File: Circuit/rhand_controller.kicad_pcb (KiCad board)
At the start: 2 copper layers, 100 x 100 mm, 39 parts, among them P1 BLUETOOTH, P10 LV_ADC, P11 LW_ADC, P12 RU_ADC, P13 RV_ADC, P14 RW_ADC, P2 CONN_01X06, P3 Wall, P4 CW, P5 Enable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

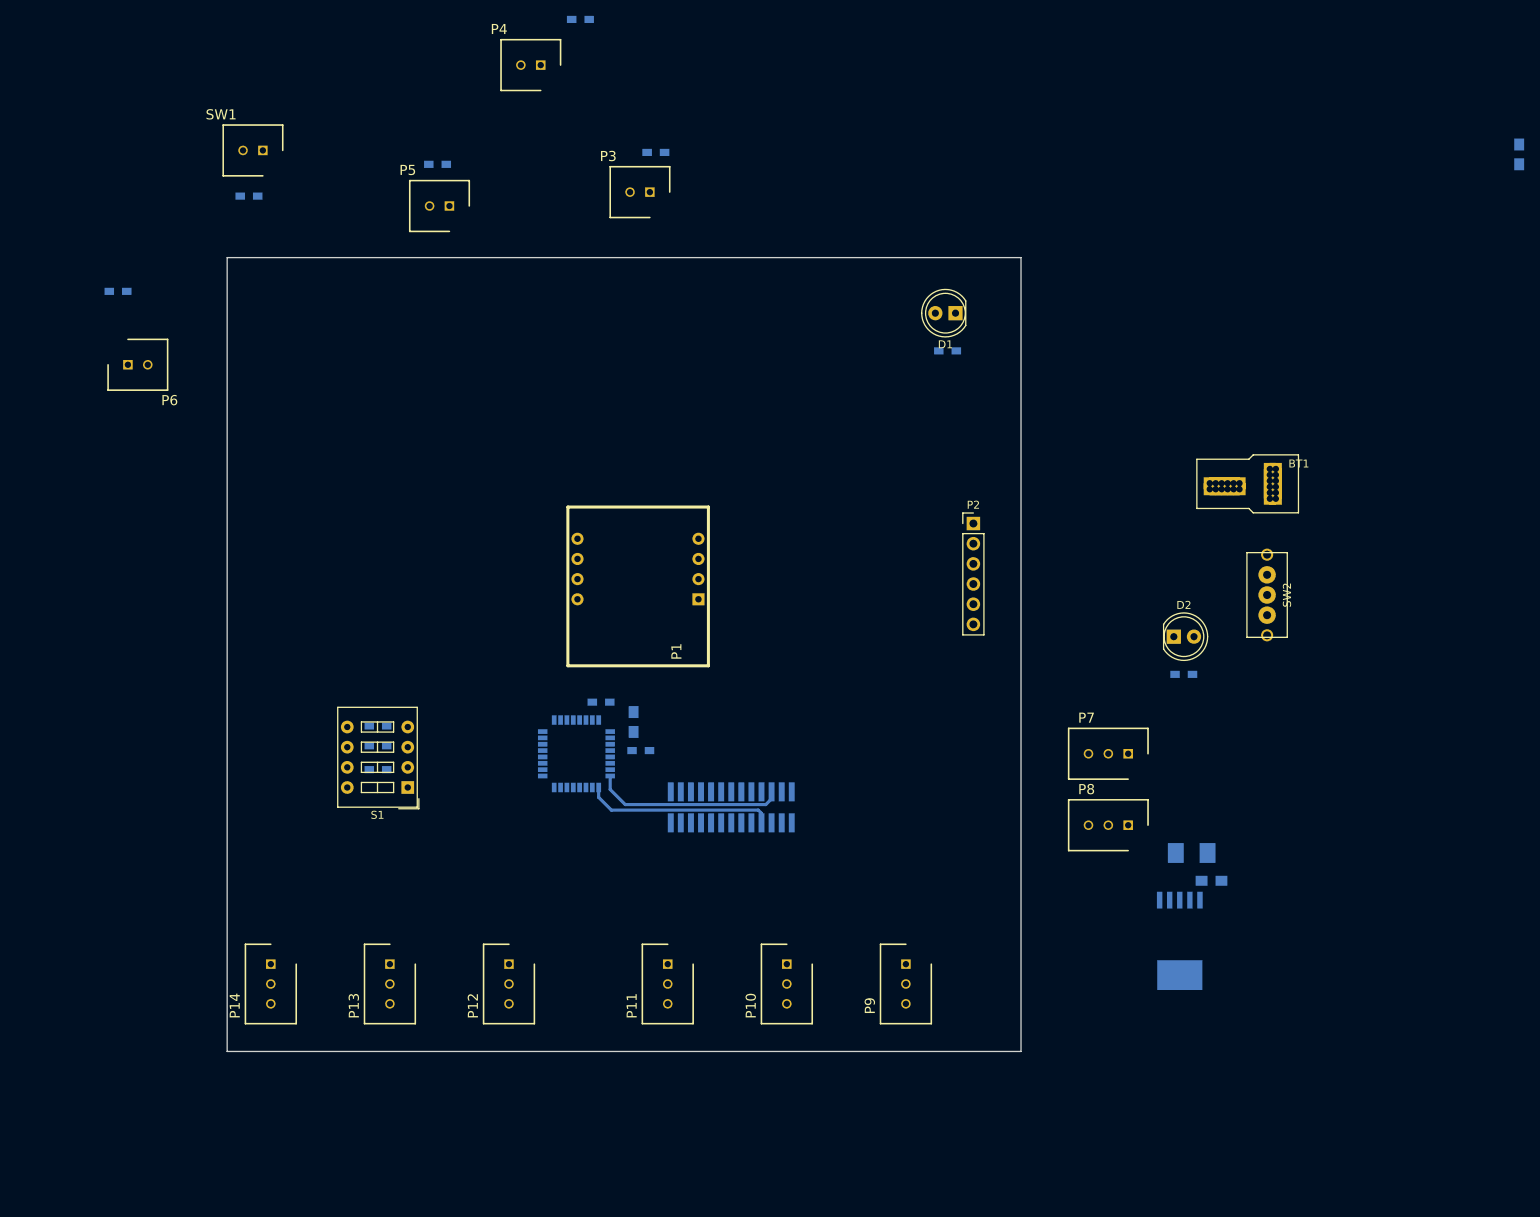
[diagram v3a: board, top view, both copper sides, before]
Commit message: ADCのピン配置修正と配線引きはじめ
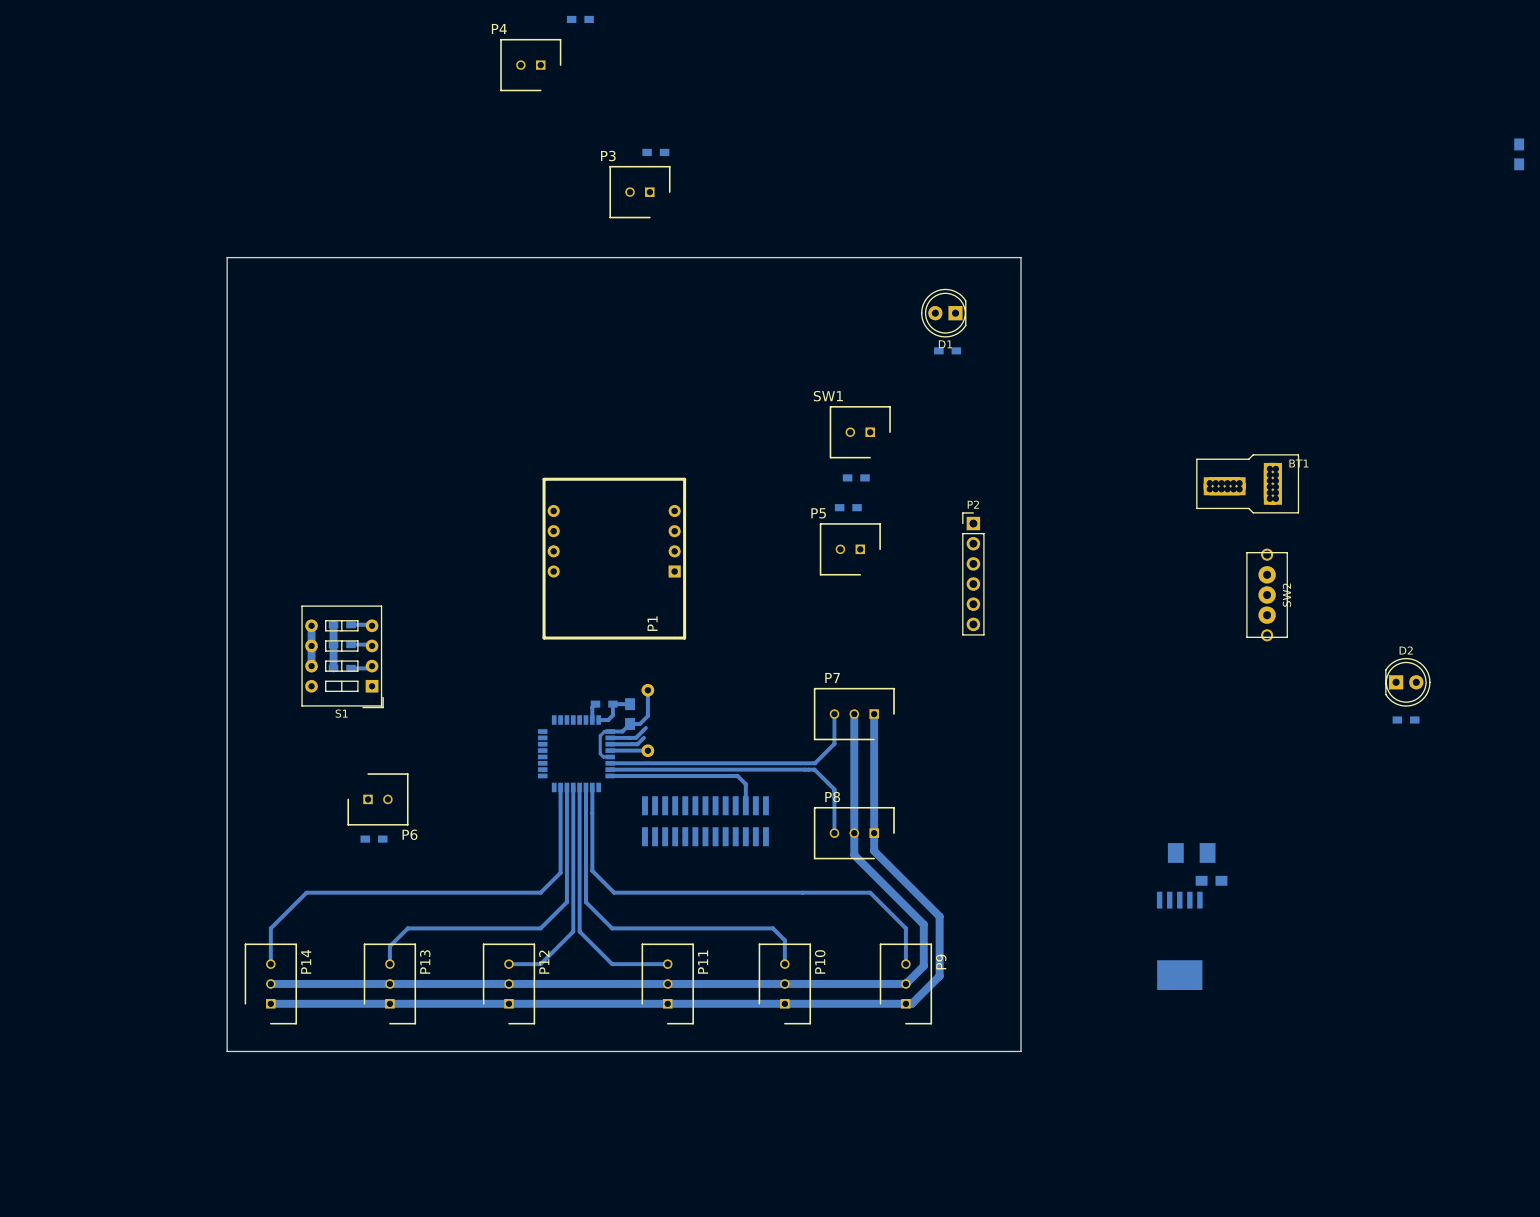
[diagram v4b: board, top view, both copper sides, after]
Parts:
- R7: footprint Resistors_SMD:R_0603_HandSoldering -> Resistors_ThroughHole:R_Axial_DIN0207_L6.3mm_D2.5mm_P7.62mm_Horizontal
- moved R4 84.3 mm to (129.2, 97.8)
- moved SW1 84.3 mm to (131.0, 92.0)
- moved R11 76.2 mm to (68.5, 143.2)
- moved P5 67.4 mm to (129.8, 106.8)
- moved R10 67.4 mm to (128.2, 101.5)
- moved P6 62.6 mm to (67.8, 138.2)
- moved P7 32.4 mm to (131.5, 127.5)
- moved P8 32.0 mm to (131.5, 142.5)
- moved D2 28.6 mm to (197.2, 123.5)
- moved R12 28.6 mm to (198.5, 128.2)
- moved R1 13.5 mm to (64.5, 116.2)
- moved R2 13.5 mm to (64.5, 118.8)
- moved R3 13.5 mm to (64.5, 121.8)
- moved S1 13.5 mm to (68.2, 124.0)
- moved R7 7.65 mm to (103.0, 124.5), turned to 270 degrees
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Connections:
- P10 pad 1: GND -> +3V3
- P10 pad 2: /LeftV -> GND
- P10 pad 3: +3V3 -> /LeftV
- P11 pad 1: GND -> +3V3
- P11 pad 2: /LeftW -> GND
- P11 pad 3: +3V3 -> /LeftW
- P12 pad 1: GND -> +3V3
- P12 pad 2: /RightU -> GND
- P12 pad 3: +3V3 -> /RightU
- P13 pad 1: GND -> +3V3
- P13 pad 2: /RightV -> GND
- P13 pad 3: +3V3 -> /RightV
- P14 pad 1: GND -> +3V3
- P14 pad 2: /RightW -> GND
- P14 pad 3: +3V3 -> /RightW
- P3 pad 1: GND -> /Wall
- P3 pad 2: /Wall -> GND
- P4 pad 1: GND -> /CW
- P4 pad 2: /CW -> GND
- P5 pad 1: GND -> /Enable
- P5 pad 2: /Enable -> GND
- P6 pad 1: GND -> /CCW
- P6 pad 2: /CCW -> GND
- P7 pad 1: GND -> +3V3
- P7 pad 2: /Joy_X -> GND
- P7 pad 3: +3V3 -> /Joy_X
- P8 pad 1: GND -> +3V3
- P8 pad 2: /Joy_Y -> GND
- P8 pad 3: +3V3 -> /Joy_Y
- P9 pad 1: GND -> +3V3
- P9 pad 2: /LeftU -> GND
- P9 pad 3: +3V3 -> /LeftU
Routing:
- net +3V3: track 0.00 -> 141.1 mm
- net GND: track 0.00 -> 129.7 mm
- net /LeftU: track 0.00 -> 57.5 mm
- net /RightW: track 0.00 -> 54.6 mm
- net /LeftV: track 0.00 -> 44.5 mm
- net /RightV: track 0.00 -> 41.3 mm
- net /Joy_Y: track 0.00 -> 34.8 mm
- net /Joy_X: track 0.00 -> 33.0 mm
- net /LeftW: track 0.00 -> 30.9 mm
- net /RightU: track 0.00 -> 27.9 mm
- net /315MHz_TXD: track 23.8 -> 0.00 mm
- net /Wall: track 0.00 -> 5.02 mm
- net /NRST: track 0.00 -> 4.76 mm
- net /Enable: track 0.00 -> 4.58 mm
- net /315MHz_RXD: track 24.0 -> 20.2 mm
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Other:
- net class Default: clearance 0.1 -> 0.15
- rule trace_clearance: 0.1 -> 0.15

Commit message: あらかた終わったぞ
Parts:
- R10, R11, R12, R4, R8, R9: footprint Resistors_SMD:R_0603_HandSoldering -> Resistors_ThroughHole:R_Axial_DIN0207_L6.3mm_D2.5mm_P7.62mm_Horizontal
- U1: moved to F.Cu
- moved P2 119.0 mm to (26.8, 123.5), turned to 90 degrees
- moved C1 114.9 mm to (118.2, 122.2), turned to 180 degrees
- moved R9 105.6 mm to (60.5, 140.0)
- moved P4 102.0 mm to (68.2, 145.5)
- moved U3 79.0 mm to (127.1, 85.1), turned to 270 degrees
- moved C3 77.7 mm to (131.0, 83.8), turned to 270 degrees
- moved BT1 72.4 mm to (113.4, 74.6)
- moved D2 71.3 mm to (139.0, 82.4), turned to 270 degrees
- moved C4 68.9 mm to (134.4, 87.0), turned to 90 degrees
- moved R4 68.5 mm to (60.8, 97.6), turned to 0 degrees
- moved SW1 65.3 mm to (65.8, 89.2), turned to 180 degrees
- moved SW2 64.9 mm to (127.7, 75.6), turned to 0 degrees
- moved R12 64.8 mm to (144.8, 92.0), turned to 180 degrees
- moved R8 61.5 mm to (142.2, 105.0)
- moved P3 47.6 mm to (134.7, 97.5), turned to 180 degrees
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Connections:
- U2 pad 29: /Blutooth_RXD -> /315MHz_RXD
- U2 pad 30: /Blutooth_TXD -> /315MHz_TXD
- U2 pad 8: /315MHz_RXD -> /Blutooth_RXD
- U2 pad 9: /315MHz_TXD -> /Blutooth_TXD
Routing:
- net GND: track 129.7 -> 349.0 mm
- net +3V3: track 141.1 -> 316.5 mm
- net /Wall: track 5.02 -> 61.2 mm
- net Net-(R4-Pad2): track 0.00 -> 48.5 mm
- net /Enable: track 4.58 -> 48.0 mm
- net /DSW_B2: track 2.70 -> 38.6 mm
- net /DSW_B1: track 2.72 -> 35.5 mm
- net /DSW_B0: track 2.77 -> 34.9 mm
- net /CW: track 0.00 -> 29.5 mm
- net /CCW: track 0.00 -> 27.9 mm
- net /busy: track 0.00 -> 26.4 mm
- net /315MHz_TXD: track 0.00 -> 25.8 mm
- net /Blutooth_RXD: track 0.00 -> 24.9 mm
- net /Blutooth_TXD: track 0.00 -> 22.9 mm
- net /reset315: track 0.00 -> 20.4 mm, vias 0 -> 2
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
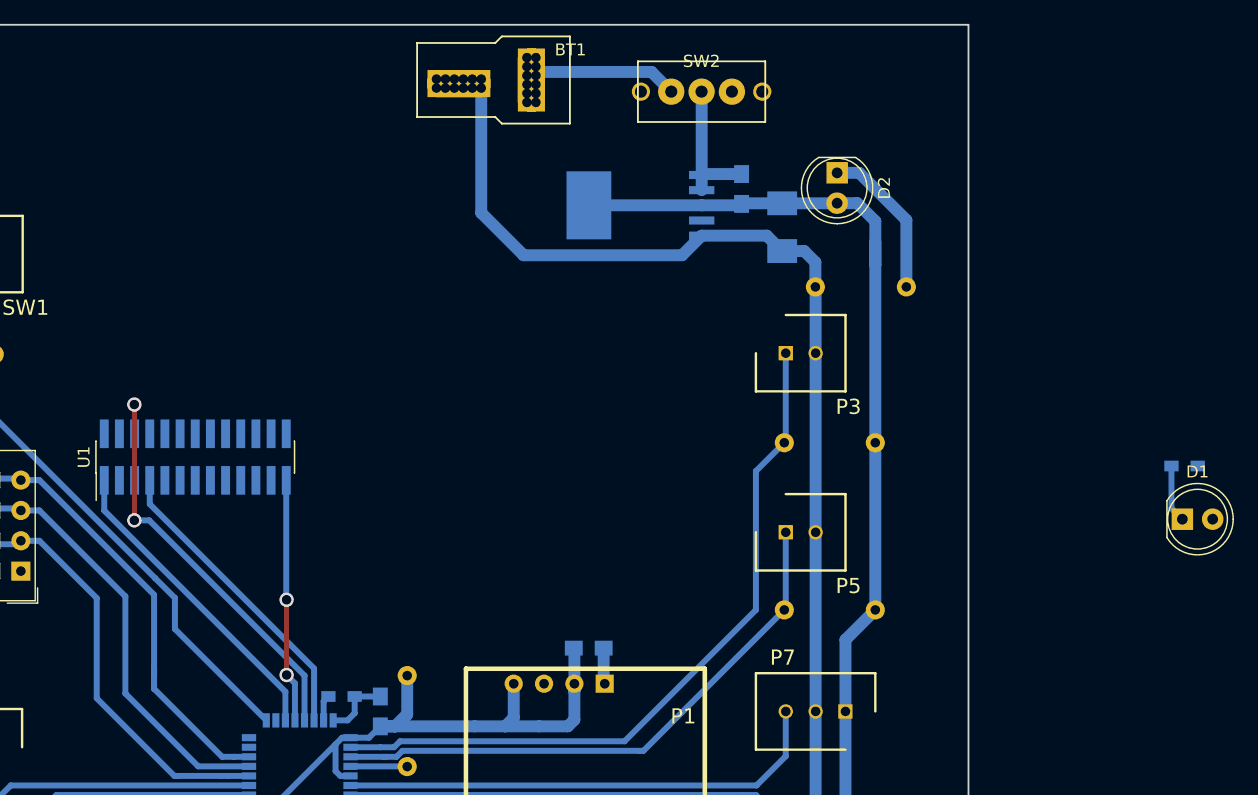
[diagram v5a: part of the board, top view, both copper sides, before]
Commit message: IM315の位置変更
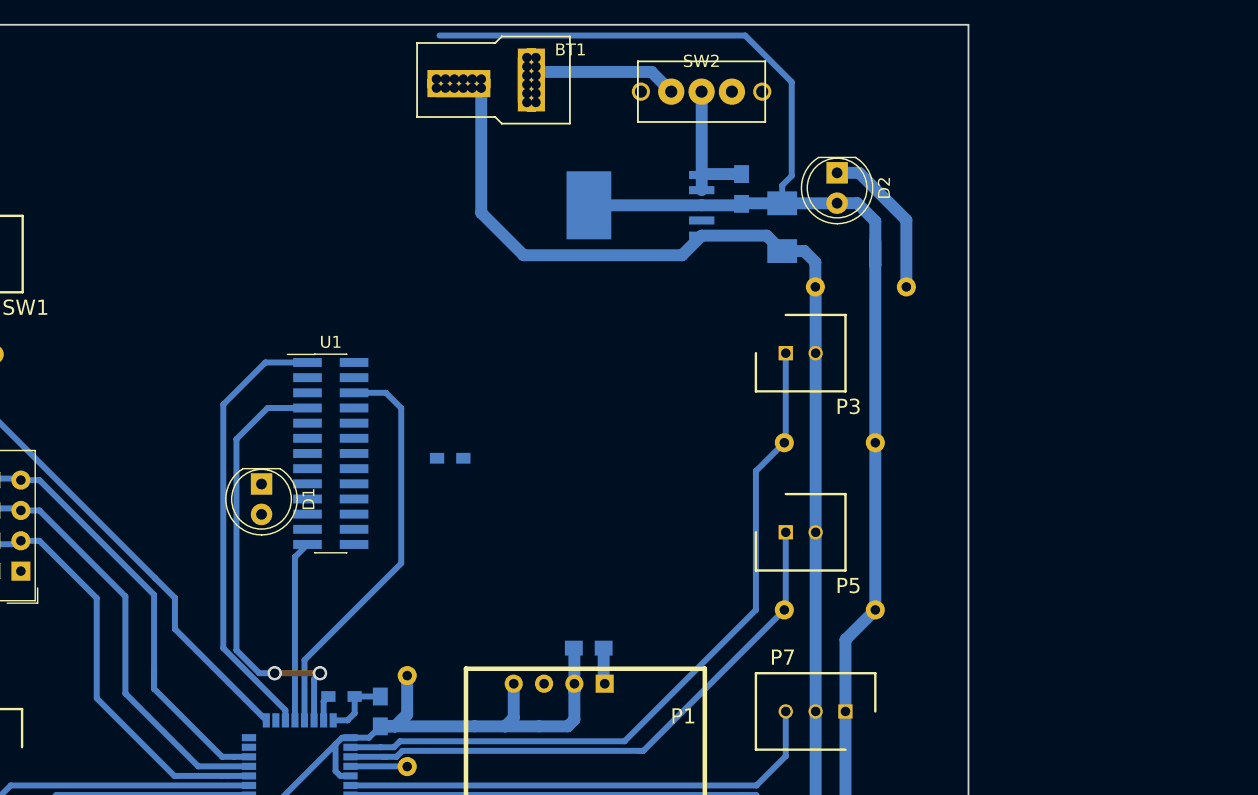
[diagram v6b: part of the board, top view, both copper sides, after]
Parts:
- moved D1 77.2 mm to (90.8, 108.5), turned to 270 degrees
- moved R5 61.5 mm to (106.6, 106.3)
- moved U1 11.4 mm to (96.6, 105.9), turned to 0 degrees
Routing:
- net +3V3: track 316.5 -> 358.1 mm
- net /315MHz_TXD: track 25.8 -> 36.7 mm, vias 0 -> 2
- net /busy: track 26.4 -> 37.1 mm
- net /reset315: track 20.4 -> 15.2 mm, vias 2 -> 0
- net Net-(D1-Pad1): track 4.83 -> 0.00 mm
- net /315MHz_RXD: track 35.5 -> 34.0 mm, vias 2 -> 0

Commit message: 作業しようと思ったらほとんどできなかった
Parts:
- moved P2 70.0 mm to (77.5, 75.4)
- moved R5 18.1 mm to (91.1, 115.6)
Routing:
- net GND: track 349.0 -> 406.6 mm
- net /315MHz_RXD: track 34.0 -> 0.00 mm
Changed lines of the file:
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@@
   (general
     (links 126)
-    (no_connects 15)
-    (area 23.495 69.924999 172.585001 170.075001)
+    (no_connects 14)
+    (area 23.495 69.924999 150.075001 170.075001)
     (thickness 1.6)
     (drawings 9)
-    (tracks 267)
+    (tracks 273)
     (zones 0)
     (modules 39)
@@
   )
   (module Resistors_SMD:R_0603_HandSoldering (layer B.Cu)
-    (at 106.6 106.3)
+    (at 91.1 115.6)
     (descr "Resistor SMD 0603, hand soldering")
     (tags "resistor 0603")
@@
   )
   (module Pin_Headers:Pin_Header_Straight_1x06_Pitch2.54mm (layer F.Cu)
-    (at 26.75 123.55 90)
+    (at 77.5 75.4 90)
     (descr "Through hole straight pin header, 1x06, 2.54mm pitch, single row")
     (tags "Through hole pin header THT 1x06 2.54mm single row")
@@
   (segment (start 114.075 73.95) (end 113.775 74.25) (width 1) (layer B.Cu) (net 1))
   (segment (start 113.775 74.25) (end 113.775 75) (width 1) (layer B.Cu) (net 1))
+  (segment (start 101.3 110.7) (end 101.3 125.7) (width 1) (layer B.Cu) (net 2) (status 800000))
+  (segment (start 101.3 125.7) (end 100.75 126.25) (width 1) (layer B.Cu) (net 2) (status C00000))
+  (segment (start 98.55 108.44) (end 100.34 108.44) (width 1) (layer B.Cu) (net 2) (status 400000))
+  (segment (start 100.55 112.25) (end 98.55 112.25) (width 1) (layer B.Cu) (net 2) (status 800000))
+  (segment (start 101.3 111.5) (end 100.55 112.25) (width 1) (layer B.Cu) (net 2))
+  (segment (start 101.3 109.4) (end 101.3 110.7) (width 1) (layer B.Cu) (net 2))
+  (segment (start 101.3 110.7) (end 101.3 111.5) (width 1) (layer B.Cu) (net 2))
+  (segment (start 100.34 108.44) (end 101.3 109.4) (width 1) (layer B.Cu) (net 2))
+  (segment (start 119.45 122.2) (end 119.45 90.95) (width 1) (layer B.Cu) (net 2))
+  (segment (start 119.45 90.95) (end 117.8 89.3) (width 1) (layer B.Cu) (net 2))
   (segment (start 137.2 97.5) (end 137.2 91.97) (width 1) (layer B.Cu) (net 2))
   (segment (start 137.2 91.97) (end 137.18 91.95) (width 1) (layer B.Cu) (net 2))
@@
   (segment (start 119.45 125.09) (end 119.54 125.18) (width 1) (layer B.Cu) (net 2))
   (segment (start 109.2 75.3) (end 109.2 85.75) (width 1) (layer B.Cu) (net 2))
+  (segment (start 109.2 85.75) (end 112.75 89.3) (width 1) (layer B.Cu) (net 2))
+  (segment (start 112.75 89.3) (end 117.8 89.3) (width 1) (layer B.Cu) (net 2))
   (segment (start 126.019 89.3) (end 127.660451 87.658549) (width 1) (layer B.Cu) (net 2))
-  (segment (start 112.75 89.3) (end 126.019 89.3) (width 1) (layer B.Cu) (net 2))
-  (segment (start 109.2 85.75) (end 112.75 89.3) (width 1) (layer B.Cu) (net 2))
+  (segment (start 117.8 89.3) (end 126.019 89.3) (width 1) (layer B.Cu) (net 2))
   (segment (start 127.660451 87.658549) (end 133.108549 87.658549) (width 1) (layer B.Cu) (net 2))
   (segment (start 133.108549 87.658549) (end 134.4 88.95) (width 1) (layer B.Cu) (net 2))
@@
   (segment (start 68 108) (end 70.52 108) (width 0.5) (layer B.Cu) (net 26))
   (segment (start 70.52 108) (end 70.65 108.13) (width 0.4) (layer B.Cu) (net 26))
-  (segment (start 94.4 128.25) (end 94.4 123.2) (width 0.5) (layer B.Cu) (net 29) (status 400000))
-  (segment (start 101.22 100.82) (end 98.55 100.82) (width 0.5) (layer B.Cu) (net 29) (status 800000))
-  (segment (start 102.5 102.1) (end 101.22 100.82) (width 0.5) (layer B.Cu) (net 29))
-  (segment (start 102.5 115.1) (end 102.5 102.1) (width 0.5) (layer B.Cu) (net 29))
-  (segment (start 94.4 123.2) (end 102.5 115.1) (width 0.5) (layer B.Cu) (net 29))
   (segment (start 88.7 104.7) (end 91.31 102.09) (width 0.5) (layer B.Cu) (net 30))
   (segment (start 91.31 102.09) (end 94.65 102.09) (width 0.5) (layer B.Cu) (net 30))
@@
   (segment (start 90.619252 124.3) (end 88.7 122.380748) (width 0.5) (layer B.Cu) (net 30))
   (segment (start 91.9 124.3) (end 90.619252 124.3) (width 0.5) (layer B.Cu) (net 30))
-  (segment (start 95.2 128.25) (end 95.2 124.8) (width 0.5) (layer B.Cu) (net 30) (status 400000))
+  (segment (start 95.2 128.25) (end 95.2 124.8) (width 0.5) (layer B.Cu) (net 30))
   (via (at 91.9 124.3) (size 1.2) (drill 0.8) (layers F.Cu B.Cu) (net 30))
   (segment (start 95.7 124.3) (end 91.9 124.3) (width 0.5) (layer F.Cu) (net 30))
@@
   (segment (start 87.6 101.8) (end 91.12 98.28) (width 0.5) (layer B.Cu) (net 31))
   (segment (start 91.12 98.28) (end 94.65 98.28) (width 0.5) (layer B.Cu) (net 31))
-  (segment (start 93.6 128.25) (end 93.6 114.57) (width 0.5) (layer B.Cu) (net 32) (status 400000))
-  (segment (start 93.6 114.57) (end 94.65 113.52) (width 0.5) (layer B.Cu) (net 32) (status 800000))
+  (segment (start 93.6 128.25) (end 93.6 114.57) (width 0.5) (layer B.Cu) (net 32))
+  (segment (start 93.6 114.57) (end 94.65 113.52) (width 0.5) (layer B.Cu) (net 32))
   (segment (start 96 128.25) (end 96 126.65) (width 0.5) (layer B.Cu) (net 36))
   (segment (start 96 126.65) (end 96.4 126.25) (width 0.5) (layer B.Cu) (net 36))
